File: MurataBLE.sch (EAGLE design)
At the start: 52 parts, among them IC1 I-5448, X1 TSW-114-02-S-S, X2 TSW-114-02-S-S

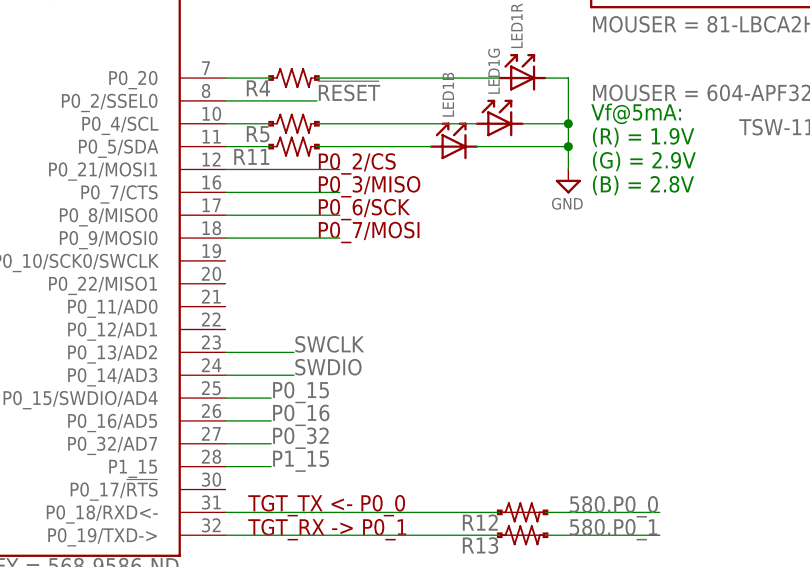
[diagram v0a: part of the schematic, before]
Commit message: [ USB ] add SWD pulp R14/15
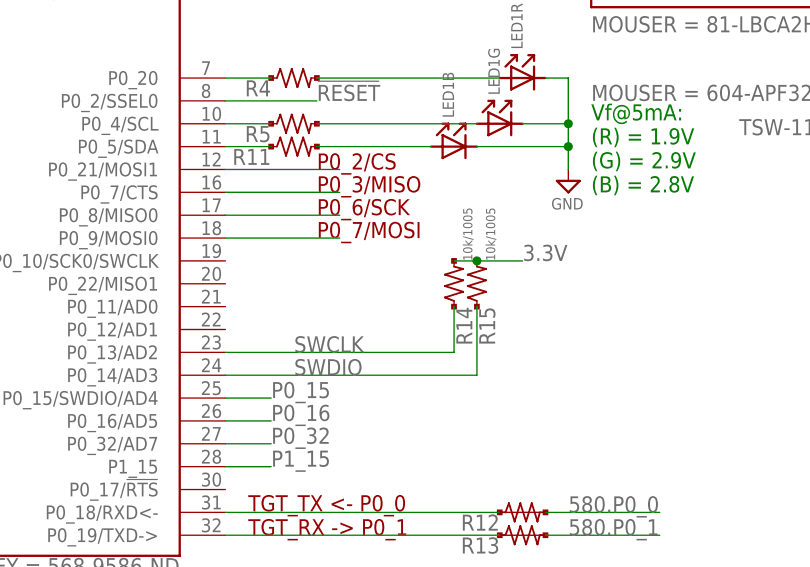
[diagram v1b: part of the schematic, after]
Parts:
- added R14, R15: 10k/1005, mylib:R_US_10K_1005
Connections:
- net 3.3V: now also R14.2, R15.2
- net SWCLK: now also R14.1
- net SWDIO: now also R15.1
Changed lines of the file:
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@@
 <attribute name="NOT_COMPONENT" value="YES"/>
 </part>
+<part name="R14" library="mylib" deviceset="R_US_*" device="_1005" technology="10K" value="10k/1005"/>
+<part name="R15" library="mylib" deviceset="R_US_*" device="_1005" technology="10K" value="10k/1005"/>
 </parts>
 <sheets>
@@
 <instance part="X2" gate="-13" x="271.78" y="63.5" rot="MR0"/>
 <instance part="X2" gate="-14" x="271.78" y="60.96" rot="MR0"/>
+<instance part="R14" gate="G$1" x="182.88" y="78.74" rot="R90"/>
+<instance part="R15" gate="G$1" x="185.42" y="78.74" rot="R90"/>
 </instances>
 <busses>
@@
 <label x="25.4" y="33.02" size="1.778" layer="95" rot="MR0"/>
 </segment>
+<segment>
+<label x="190.5" y="81.28" size="1.778" layer="95"/>
+<pinref part="R14" gate="G$1" pin="2"/>
+<wire x1="182.88" y1="81.28" x2="185.42" y2="81.28" width="0.1524" layer="91"/>
+<pinref part="R15" gate="G$1" pin="2"/>
+<wire x1="185.42" y1="81.28" x2="190.5" y2="81.28" width="0.1524" layer="91"/>
+<junction x="185.42" y="81.28"/>
+</segment>
 </net>
 <net name="RESET" class="0">
@@
 </segment>
 <segment>
-<wire x1="157.48" y1="71.12" x2="165.1" y2="71.12" width="0.1524" layer="91"/>
 <pinref part="IC2" gate="G$1" pin="P0_13/AD2"/>
 <label x="165.1" y="71.12" size="1.778" layer="95"/>
+<pinref part="R14" gate="G$1" pin="1"/>
+<wire x1="157.48" y1="71.12" x2="182.88" y2="71.12" width="0.1524" layer="91"/>
+<wire x1="182.88" y1="71.12" x2="182.88" y2="76.2" width="0.1524" layer="91"/>
 </segment>
 </net>
@@
 </segment>
 <segment>
-<wire x1="157.48" y1="68.58" x2="165.1" y2="68.58" width="0.1524" layer="91"/>
 <pinref part="IC2" gate="G$1" pin="P0_14/AD3"/>
 <label x="165.1" y="68.58" size="1.778" layer="95"/>
-</segment>
-</net>
+<pinref part="R15" gate="G$1" pin="1"/>
+<wire x1="157.48" y1="68.58" x2="185.42" y2="68.58" width="0.1524" layer="91"/>
+<wire x1="185.42" y1="68.58" x2="185.42" y2="76.2" width="0.1524" layer="91"/>
+</segment>
+</net>

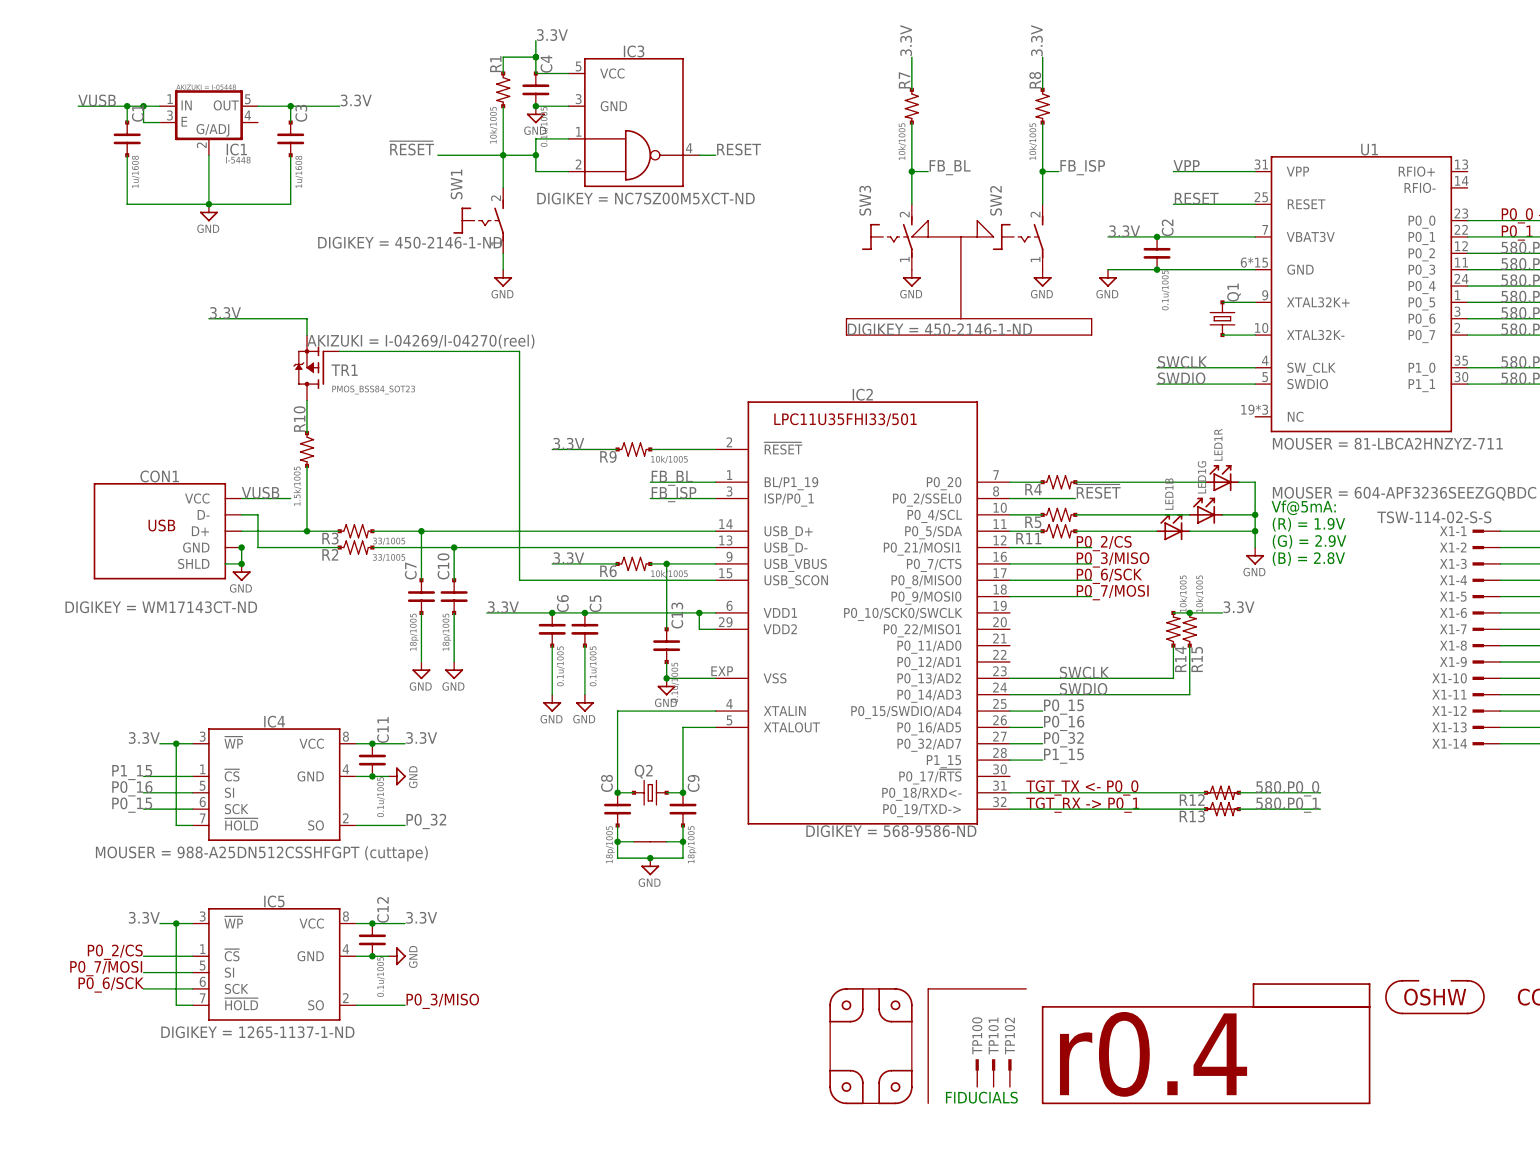
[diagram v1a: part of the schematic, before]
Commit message: [ USB ]add values; panelized
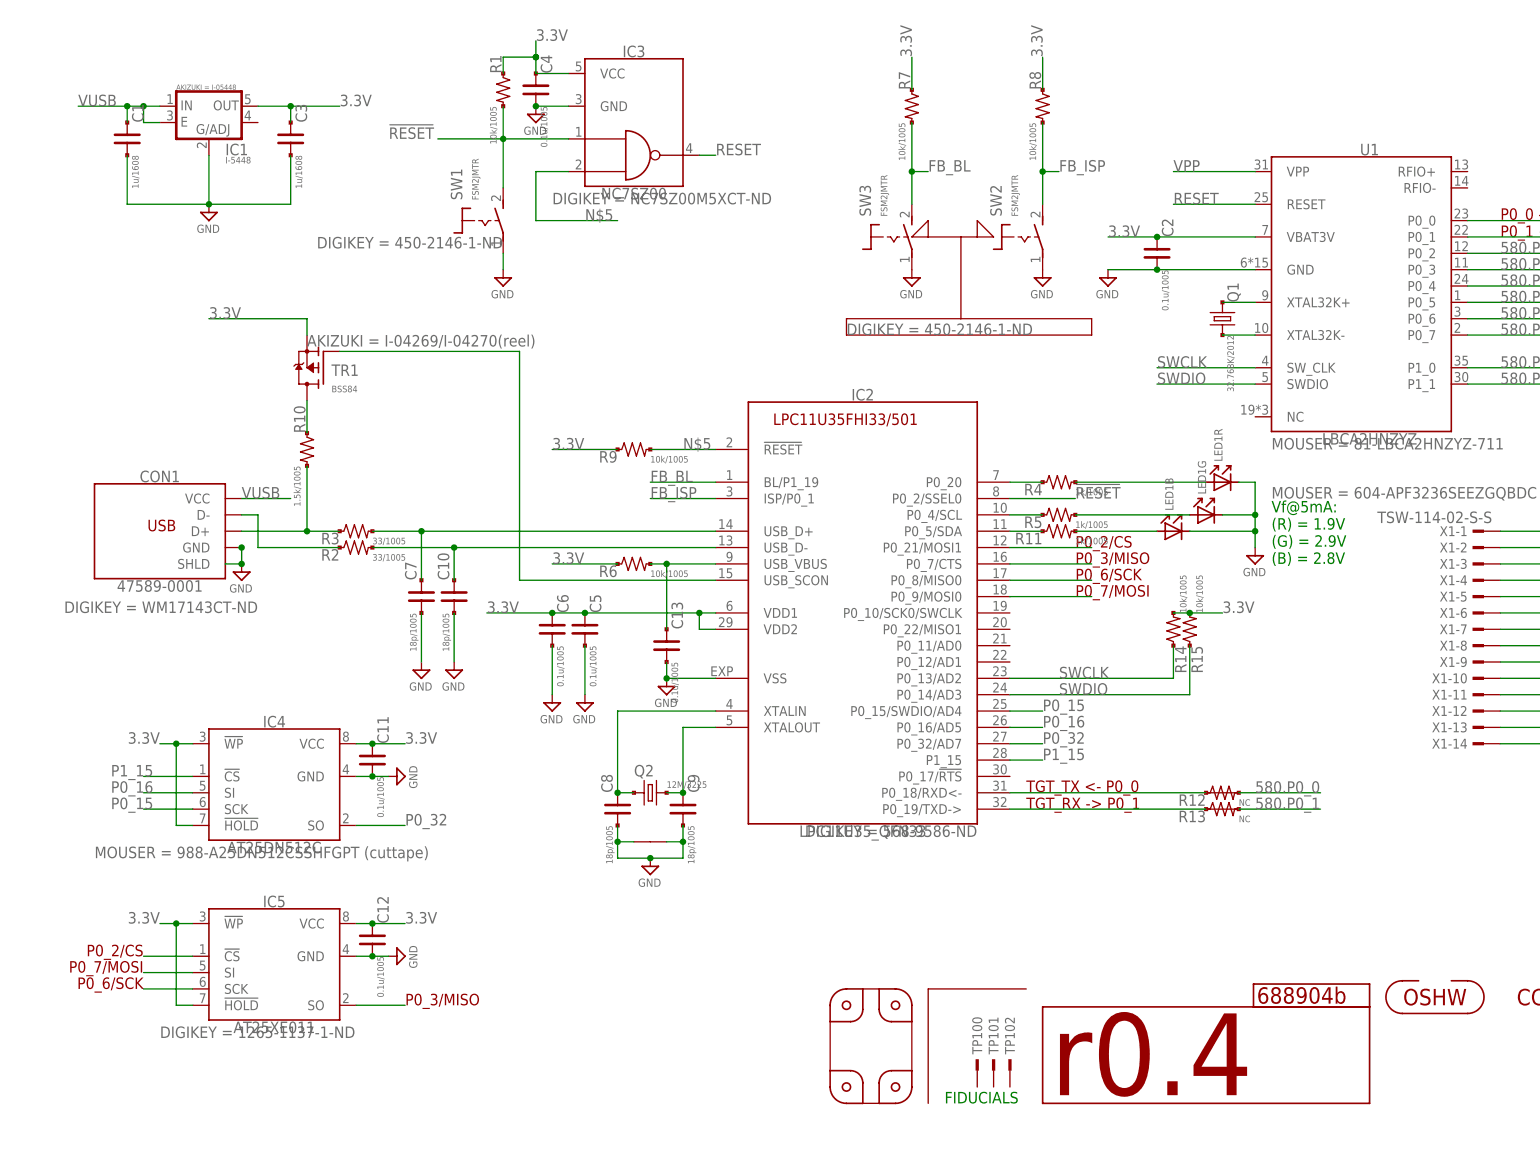
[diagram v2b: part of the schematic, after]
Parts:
- CON1: value (none) -> 47589-0001
- GIT1: value (none) -> 688904b
- IC2: value (none) -> LPC11U35_QFN33
- IC3: value (none) -> NC7SZ00
- IC4: value (none) -> AT25DN512C
- IC5: value (none) -> AT25XE011
- ICON2, P1, P2, P3, P4, R12, R13: value (none) -> NC
- Q1: value (none) -> 32.768K/2012
- Q2: value (none) -> 12M/3225
- R11, R4, R5: value (none) -> 1k/1005
- SW1, SW2, SW3: value (none) -> FSM2JMTR
- TP100, TP101, TP102: value TESTPAD_F -> NC
- TR1: value PMOS_BSS84_SOT23 -> BSS84
- U1: value (none) -> LBCA2HNZYZ
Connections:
- net !RESET!: no longer IC3.1B
- net N$5: now also IC3.1B
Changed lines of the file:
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@@
 <parts>
 <part name="FRAME1" library="frames" deviceset="A4L-LOC" device=""/>
-<part name="U1" library="mylib" deviceset="LBCA2HNZYZ-711" device=""/>
+<part name="U1" library="mylib" deviceset="LBCA2HNZYZ-711" device="" value="LBCA2HNZYZ"/>
 <part name="SUPPLY1" library="mylib" deviceset="GND" device=""/>
-<part name="Q1" library="mylib" deviceset="CRYSTAL2_*" device="_2012" technology="32.768K"/>
+<part name="Q1" library="mylib" deviceset="CRYSTAL2_*" device="_2012" technology="32.768K" value="32.768K/2012"/>
 <part name="C2" library="mylib" deviceset="C_SMD_*" device="_1005" technology="0.1U" value="0.1u/1005"/>
-<part name="SW1" library="mylib" deviceset="TACTSW2_*" device="FSM2JMTR"/>
+<part name="SW1" library="mylib" deviceset="TACTSW2_*" device="FSM2JMTR" value="FSM2JMTR"/>
 <part name="R1" library="mylib" deviceset="R_US_*" device="_1005" technology="10K" value="10k/1005"/>
 <part name="C1" library="mylib" deviceset="C_SMD_*" device="_1608" technology="1.0U" value="1u/1608"/>
@@
 <part name="R2" library="mylib" deviceset="R_US_*" device="_1005" technology="33R" value="33/1005"/>
 <part name="R3" library="mylib" deviceset="R_US_*" device="_1005" technology="33R" value="33/1005"/>
-<part name="SW2" library="mylib" deviceset="TACTSW2_*" device="FSM2JMTR"/>
-<part name="SW3" library="mylib" deviceset="TACTSW2_*" device="FSM2JMTR"/>
+<part name="SW2" library="mylib" deviceset="TACTSW2_*" device="FSM2JMTR" value="FSM2JMTR"/>
+<part name="SW3" library="mylib" deviceset="TACTSW2_*" device="FSM2JMTR" value="FSM2JMTR"/>
 <part name="SUPPLY8" library="mylib" deviceset="GND" device=""/>
 <part name="SUPPLY9" library="mylib" deviceset="GND" device=""/>
@@
 <part name="SUPPLY14" library="mylib" deviceset="GND" device=""/>
 <part name="SUPPLY15" library="mylib" deviceset="GND" device=""/>
-<part name="TR1" library="mylib" deviceset="PMOS_*" device="_SOT23" technology="BSS84" value="PMOS_BSS84_SOT23"/>
+<part name="TR1" library="mylib" deviceset="PMOS_*" device="_SOT23" technology="BSS84" value="BSS84"/>
 <part name="R10" library="mylib" deviceset="R_US_*" device="_1005" technology="1.5K" value="1.5k/1005"/>
-<part name="R4" library="mylib" deviceset="R_US_*" device="_1005" technology="1.0K"/>
-<part name="R5" library="mylib" deviceset="R_US_*" device="_1005" technology="1.0K"/>
-<part name="R11" library="mylib" deviceset="R_US_*" device="_1005" technology="1.0K"/>
+<part name="R4" library="mylib" deviceset="R_US_*" device="_1005" technology="1.0K" value="1k/1005"/>
+<part name="R5" library="mylib" deviceset="R_US_*" device="_1005" technology="1.0K" value="1k/1005"/>
+<part name="R11" library="mylib" deviceset="R_US_*" device="_1005" technology="1.0K" value="1k/1005"/>
 <part name="SUPPLY16" library="mylib" deviceset="GND" device=""/>
 <part name="LED1" library="mylib" deviceset="LED_3SEG" device=""/>
@@
 <attribute name="NOT_COMPONENT" value="YES"/>
 </part>
-<part name="TP100" library="mylib" deviceset="TESTPAD" device="_F" value="TESTPAD_F"/>
-<part name="TP101" library="mylib" deviceset="TESTPAD" device="_F" value="TESTPAD_F"/>
-<part name="TP102" library="mylib" deviceset="TESTPAD" device="_F" value="TESTPAD_F"/>
-<part name="Q2" library="mylib" deviceset="CRYSTAL4_*" device="_3225" technology="12M"/>
-<part name="IC4" library="mylib" deviceset="IC_MEMORY_8P_*" device="_SOP" technology="AT25DN512C"/>
-<part name="IC5" library="mylib" deviceset="IC_MEMORY_8P_*" device="_SOP" technology="AT25XE011"/>
-<part name="IC2" library="mylib" deviceset="IC_LPC11U*_QFN33" device="_5X5" technology="35"/>
+<part name="TP100" library="mylib" deviceset="TESTPAD" device="_F" value="NC"/>
+<part name="TP101" library="mylib" deviceset="TESTPAD" device="_F" value="NC"/>
+<part name="TP102" library="mylib" deviceset="TESTPAD" device="_F" value="NC"/>
+<part name="Q2" library="mylib" deviceset="CRYSTAL4_*" device="_3225" technology="12M" value="12M/3225"/>
+<part name="IC4" library="mylib" deviceset="IC_MEMORY_8P_*" device="_SOP" technology="AT25DN512C" value="AT25DN512C"/>
+<part name="IC5" library="mylib" deviceset="IC_MEMORY_8P_*" device="_SOP" technology="AT25XE011" value="AT25XE011"/>
+<part name="IC2" library="mylib" deviceset="IC_LPC11U*_QFN33" device="_5X5" technology="35" value="LPC11U35_QFN33"/>
 <part name="SUPPLY17" library="mylib" deviceset="GND" device=""/>
 <part name="SUPPLY18" library="mylib" deviceset="GND" device=""/>
@@
 <part name="C12" library="mylib" deviceset="C_SMD_*" device="_1005" technology="0.1U" value="0.1u/1005"/>
 <part name="ICON1" library="mylib" deviceset="ICON_REVISION" device="_1.2" value="r0.4"/>
-<part name="ICON2" library="mylib" deviceset="ICON_OSHW" device=""/>
-<part name="CON1" library="mylib" deviceset="CON_USB" device="_UB"/>
-<part name="P1" library="mylib" deviceset="PCB_CORNER" device="_NH"/>
-<part name="P2" library="mylib" deviceset="PCB_CORNER" device="_NH"/>
-<part name="P3" library="mylib" deviceset="PCB_CORNER" device="_NH"/>
-<part name="P4" library="mylib" deviceset="PCB_CORNER" device="_NH"/>
+<part name="ICON2" library="mylib" deviceset="ICON_OSHW" device="" value="NC"/>
+<part name="CON1" library="mylib" deviceset="CON_USB" device="_UB" value="47589-0001"/>
+<part name="P1" library="mylib" deviceset="PCB_CORNER" device="_NH" value="NC"/>
+<part name="P2" library="mylib" deviceset="PCB_CORNER" device="_NH" value="NC"/>
+<part name="P3" library="mylib" deviceset="PCB_CORNER" device="_NH" value="NC"/>
+<part name="P4" library="mylib" deviceset="PCB_CORNER" device="_NH" value="NC"/>
 <part name="C13" library="mylib" deviceset="C_SMD_*" device="_1005" technology="0.1U" value="0.1u/1005"/>
-<part name="R12" library="mylib" deviceset="R_US_*" device="_1005SHORT"/>
-<part name="R13" library="mylib" deviceset="R_US_*" device="_1005SHORT"/>
-<part name="IC3" library="mylib" deviceset="IC_TTL_SINGLE_74_00" device="_SOT23"/>
-<part name="GIT1" library="git-revision" deviceset="GIT-REVISION" device=""/>
+<part name="R12" library="mylib" deviceset="R_US_*" device="_1005SHORT" value="NC"/>
+<part name="R13" library="mylib" deviceset="R_US_*" device="_1005SHORT" value="NC"/>
+<part name="IC3" library="mylib" deviceset="IC_TTL_SINGLE_74_00" device="_SOT23" value="NC7SZ00"/>
+<part name="GIT1" library="git-revision" deviceset="GIT-REVISION" device="" value="688904b"/>
 <part name="X2" library="mylib" deviceset="TSW-114-02-S-S" device="" value="TSW-114-02-S-S">
 <attribute name="NOT_COMPONENT" value="YES"/>
@@
 <instance part="R13" gate="G$1" x="190.5" y="50.8"/>
 <instance part="IC3" gate="G$1" x="99.06" y="157.48">
-<attribute name="DIGIKEY" x="83.82" y="144.78" size="1.778" layer="96" display="both"/>
+<attribute name="DIGIKEY" x="86.36" y="144.78" size="1.778" layer="96" display="both"/>
 </instance>
 <instance part="GIT1" gate="G$1" x="195.58" y="20.32"/>
@@
 </segment>
 <segment>
-<wire x1="68.58" y1="152.4" x2="78.74" y2="152.4" width="0.1524" layer="91"/>
-<label x="60.96" y="152.4" size="1.778" layer="95"/>
+<wire x1="68.58" y1="154.94" x2="78.74" y2="154.94" width="0.1524" layer="91"/>
+<label x="60.96" y="154.94" size="1.778" layer="95"/>
 <pinref part="R1" gate="G$1" pin="2"/>
-<wire x1="78.74" y1="152.4" x2="83.82" y2="152.4" width="0.1524" layer="91"/>
-<wire x1="78.74" y1="160.02" x2="78.74" y2="152.4" width="0.1524" layer="91"/>
-<junction x="78.74" y="152.4"/>
+<wire x1="78.74" y1="160.02" x2="78.74" y2="154.94" width="0.1524" layer="91"/>
+<junction x="78.74" y="154.94"/>
 <pinref part="SW1" gate="G$1" pin="S"/>
-<wire x1="78.74" y1="152.4" x2="78.74" y2="147.32" width="0.1524" layer="91"/>
-<wire x1="83.82" y1="149.86" x2="83.82" y2="152.4" width="0.1524" layer="91"/>
-<wire x1="83.82" y1="154.94" x2="83.82" y2="152.4" width="0.1524" layer="91"/>
-<junction x="83.82" y="152.4"/>
+<wire x1="78.74" y1="154.94" x2="78.74" y2="147.32" width="0.1524" layer="91"/>
 <pinref part="IC3" gate="G$1" pin="1A"/>
-<wire x1="83.82" y1="154.94" x2="88.9" y2="154.94" width="0.1524" layer="91"/>
-<pinref part="IC3" gate="G$1" pin="1B"/>
-<wire x1="88.9" y1="149.86" x2="83.82" y2="149.86" width="0.1524" layer="91"/>
+<wire x1="78.74" y1="154.94" x2="88.9" y2="154.94" width="0.1524" layer="91"/>
 </segment>
 </net>
@@
 <wire x1="101.6" y1="106.68" x2="111.76" y2="106.68" width="0.1524" layer="91"/>
 <pinref part="IC2" gate="G$1" pin="!RESET!"/>
-</segment>
-</net>
+<label x="106.68" y="106.68" size="1.778" layer="95"/>
+</segment>
+<segment>
+<wire x1="83.82" y1="142.24" x2="96.52" y2="142.24" width="0.1524" layer="91"/>
+<pinref part="IC3" gate="G$1" pin="1B"/>
+<wire x1="88.9" y1="149.86" x2="83.82" y2="149.86" width="0.1524" layer="91"/>
+<wire x1="83.82" y1="149.86" x2="83.82" y2="142.24" width="0.1524" layer="91"/>
+<label x="91.44" y="142.24" size="1.778" layer="95"/>
+</segment>
+</net>
